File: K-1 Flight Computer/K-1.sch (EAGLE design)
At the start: 8 parts, among them IC1 BMP280

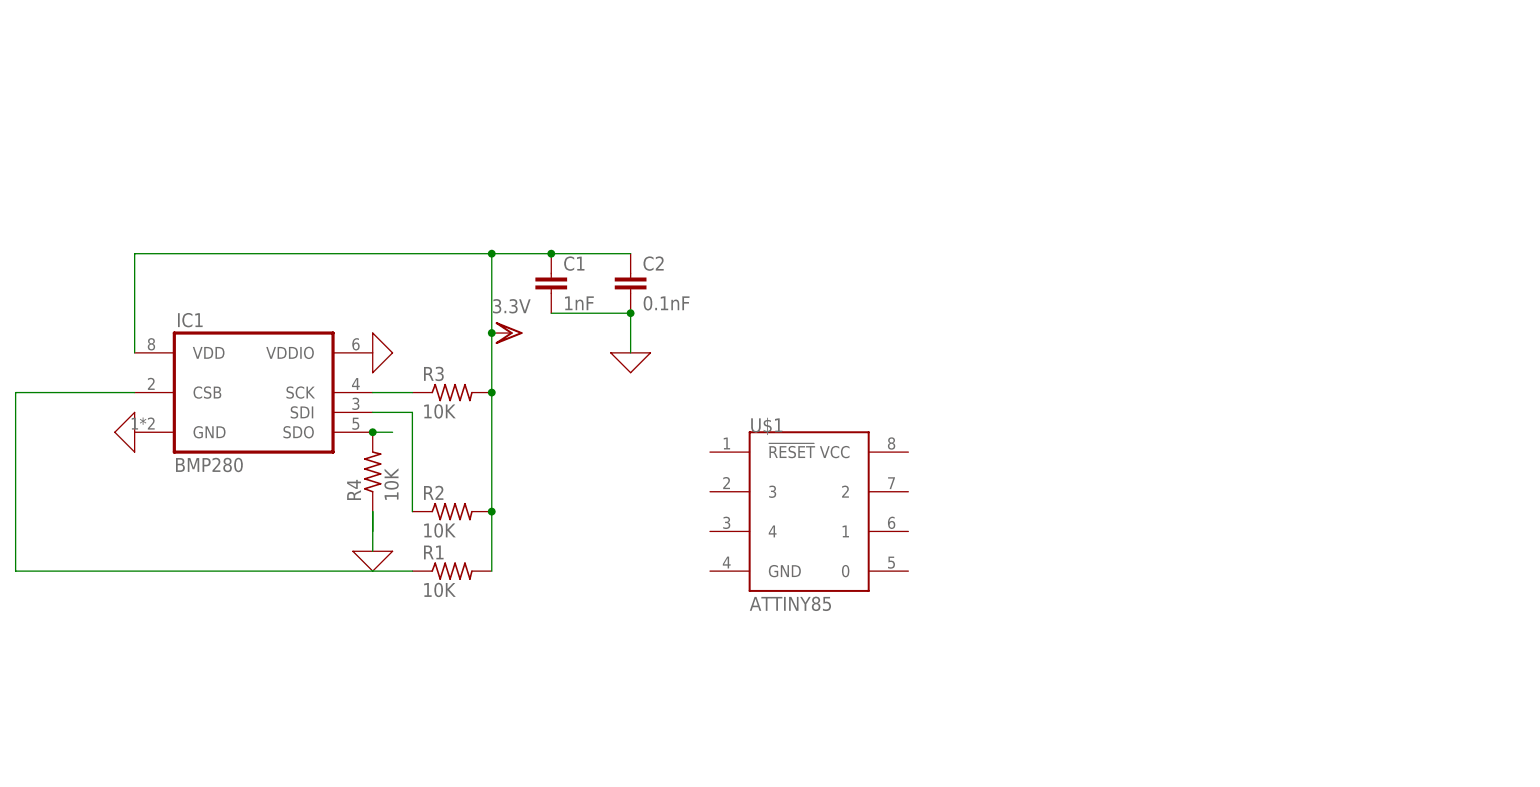
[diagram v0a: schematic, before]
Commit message: Wire voltage regulation and switch circuits and add most nessecary components
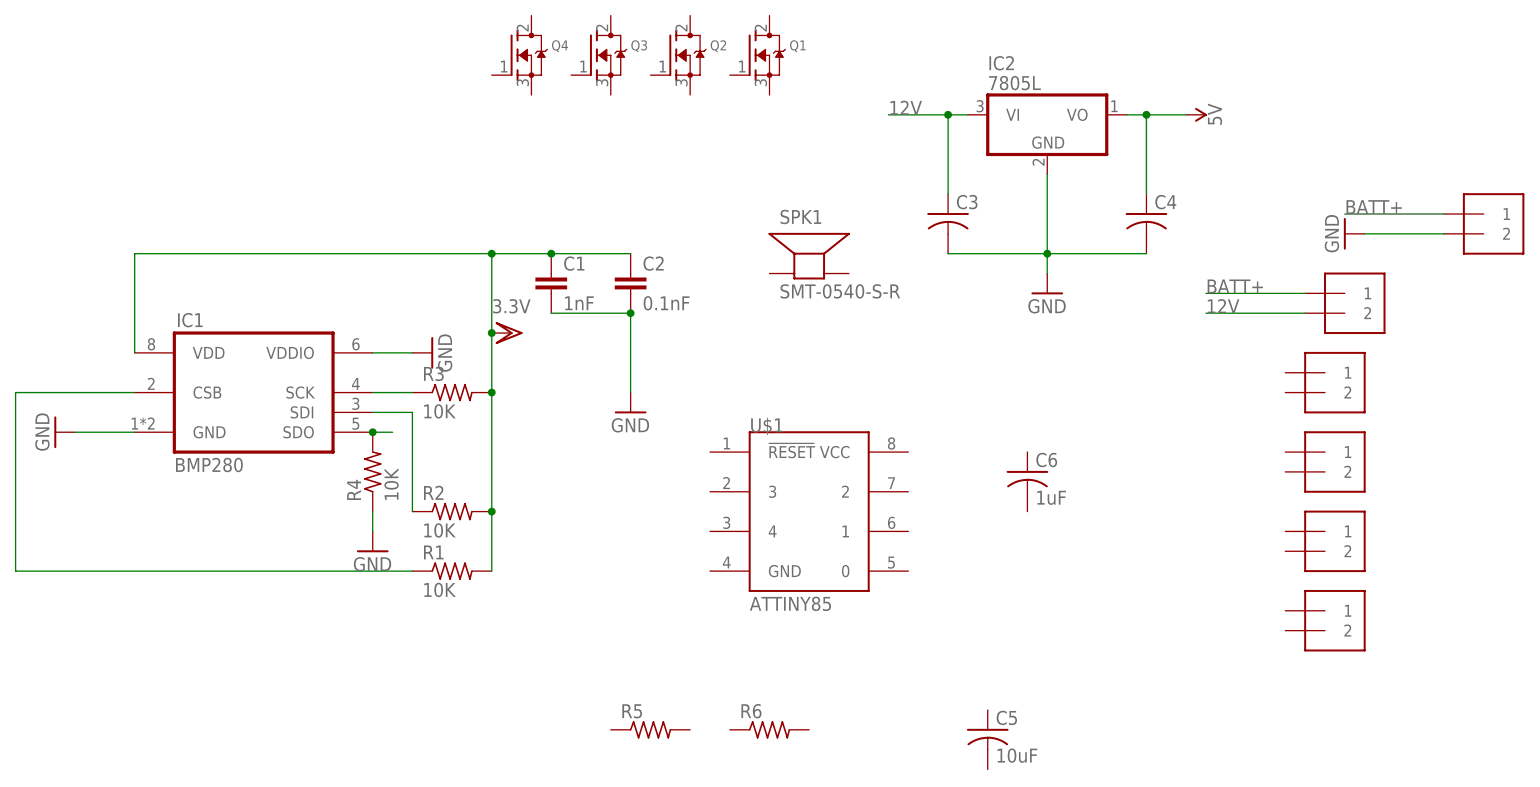
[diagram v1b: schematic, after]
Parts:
- added C3, C4: (no value), adafruit:C-US025-024X044
- added C5: 10uF, adafruit:C-US025-024X044
- added C6: 1uF, adafruit:C-US025-024X044
- added IC2: 7805L, adafruit:7805L
- added J1, J2, J3, J4, J5, J6: 1X2-3.5MM, adafruit:1X2-3.5MM
- added Q1, Q2, Q3, Q4: (no value), adafruit:MOSFET-NGDS_TO220V
- added R5, R6: (no value), adafruit:R-US_0204/2V
- added SPK1: SMT-0540-S-R, adafruit:SMT-0540-S-R
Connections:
- removed net 0: C1.2, C2.2, IC1.GND, IC1.VDDIO
- removed net N$6: R4.1
- new net 12V: C3.1, IC2.VI, J2.2
- new net 5V: C4.1, IC2.VO
- new net BATT+: J1.1, J2.1
- new net GND: C1.2, C2.2, C3.2, C4.2, IC1.GND, IC1.VDDIO, IC2.GND, J1.2, R4.1

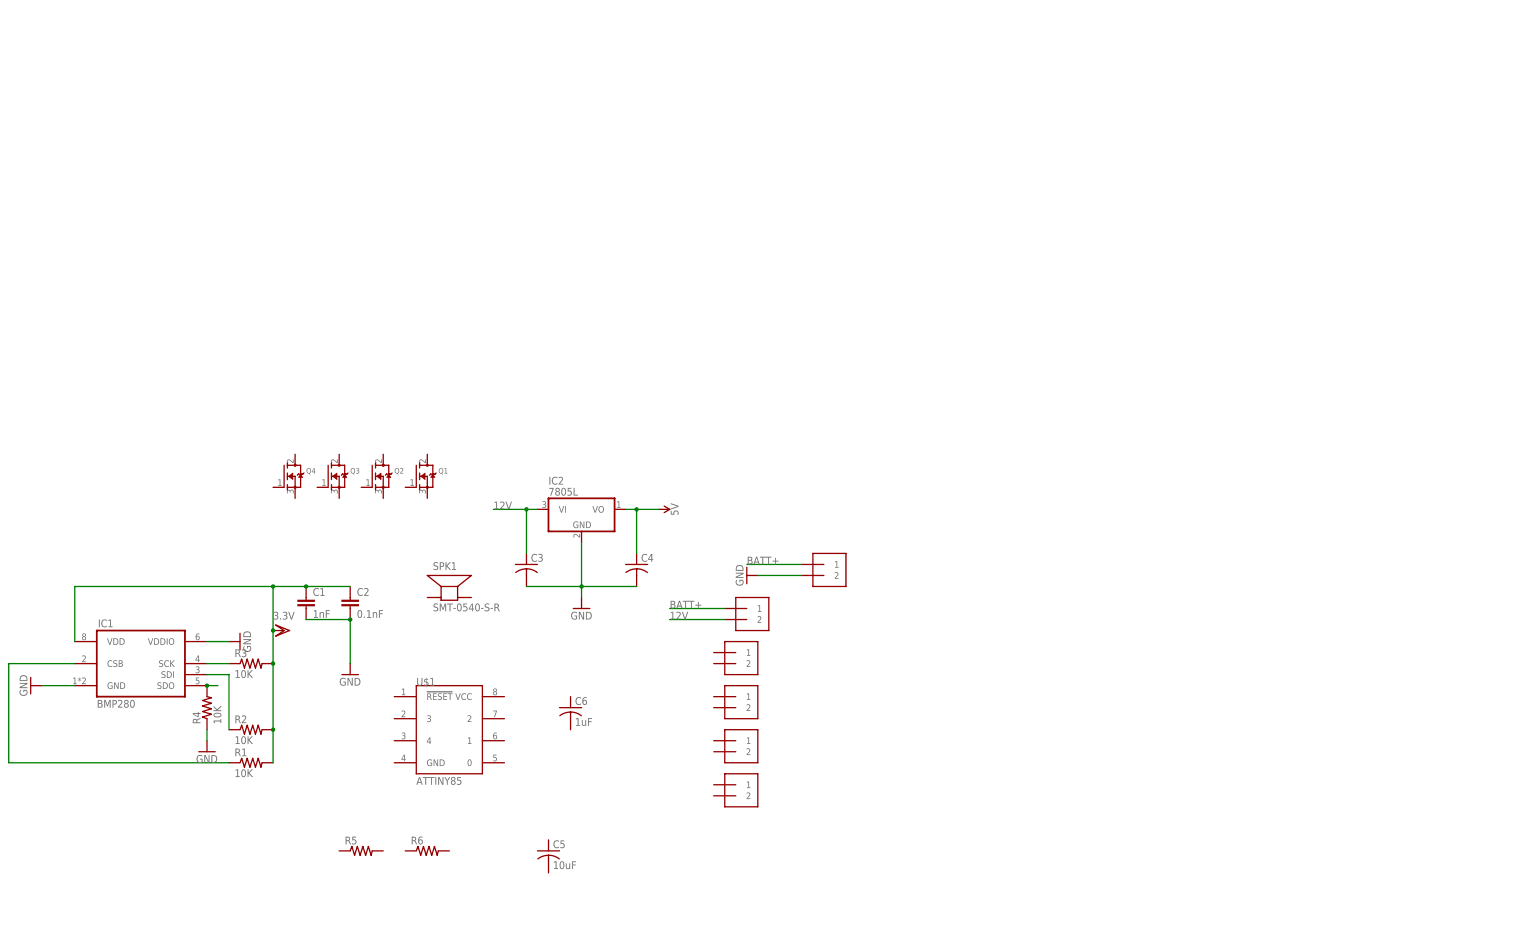
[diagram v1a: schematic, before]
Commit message: wire all components in flight computer schematics
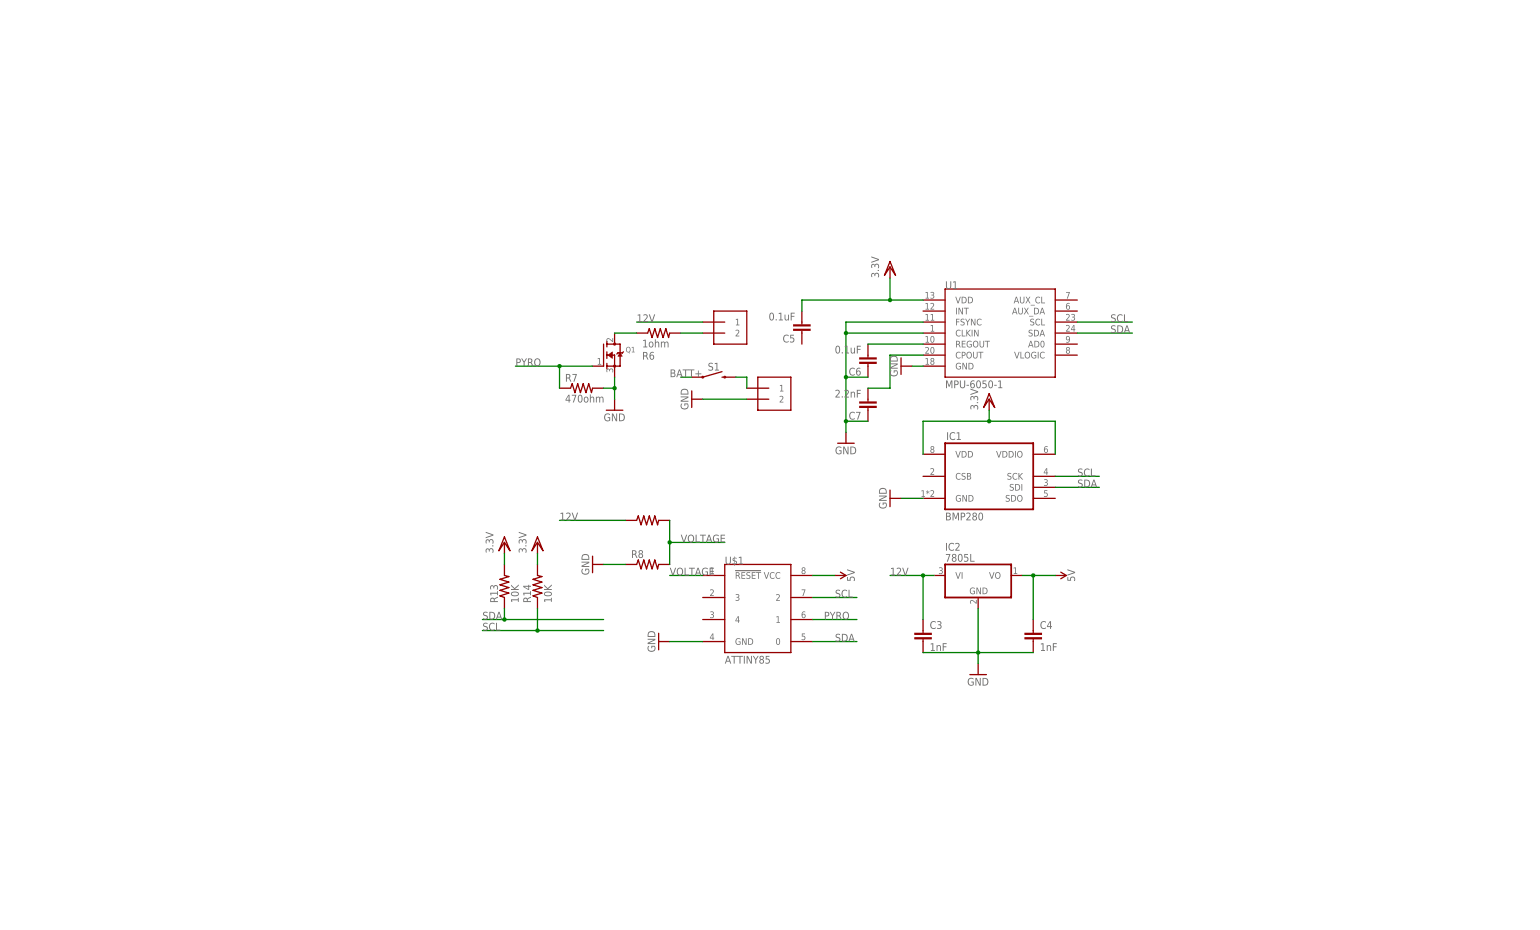
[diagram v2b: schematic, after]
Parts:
- removed C1: 1nF, capacitor-wima:C2,5-3
- removed C2: 0.1nF, capacitor-wima:C2,5-3
- removed J2, J3, J4, J5: 1X2-3.5MM, adafruit:1X2-3.5MM
- removed Q2, Q3, Q4: (no value), adafruit:MOSFET-NGDS_TO220V
- removed R1, R2, R3, R4: 10K, rcl:R-US_0204/2V
- removed SPK1: SMT-0540-S-R, adafruit:SMT-0540-S-R
- added C7: 2.2nF, capacitor-wima:C2,5-3
- added R13, R14: 10K, rcl:R-US_0204/2V
- added R7: 470ohm, adafruit:R-US_0204/2V
- added R8: (no value), adafruit:R-US_0204/2V
- added S1: MOMENTARY-SWITCH-SPST-SMD-5.2-REDUNDANT, SparkFun-Switches:MOMENTARY-SWITCH-SPST-SMD-5.2-REDUNDANT
- added U1: MPU-6050-1, Testing:MPU-6050-1
- C3, C4: value (none) -> 1nF; device adafruit:C-US025-024X044 -> capacitor-wima:C2,5-3
- C5: value 10uF -> 0.1uF; device adafruit:C-US025-024X044 -> capacitor-wima:C2,5-3
- C6: value 1uF -> 0.1uF; device adafruit:C-US025-024X044 -> capacitor-wima:C2,5-3
- R6: value (none) -> 1ohm
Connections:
- removed net N$1: IC1.CSB, R1.1
- removed net N$2: IC1.SDI, R2.1
- removed net N$3: IC1.SCK, R3.1
- removed net N$5: IC1.SDO, R4.2
- new net N$11: C7.2, U1.CPOUT
- new net N$12: C6.2, U1.REGOUT
- new net N$15: J1.1, S1.2
- new net N$4: J6.2, R6.2
- new net N$6: Q1.D, R6.1
- new net PYRO: Q1.G, R7.1, U$1.1
- new net SCL: IC1.SCK, R14.1, U$1.2, U1.SCL
- new net SDA: IC1.SDI, R13.1, U$1.0, U1.SDA
- new net VOLTAGE: R5.2, R8.2, U$1.!RESET
- net 12V: now also J6.1, R5.1; no longer J2.2
- net 5V: now also U$1.VCC
- net BATT+: now also S1.1; no longer J1.1, J2.1
- net GND: now also C6.1, C7.1, Q1.S, R7.2, R8.1, U$1.GND, U1.CLKIN, U1.FSYNC, U1.GND; no longer C1.2, C2.2, IC1.VDDIO, R4.1
- net VDD: now also C5.2, IC1.VDDIO, R13.2, R14.2, U1.VDD; no longer C1.1, C2.1, R1.2, R2.2, R3.2
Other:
- moved on the sheet: C3, C4, C5, C6, IC1, IC2, Q1, R6, U$1
